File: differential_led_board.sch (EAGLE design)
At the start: 59 parts, among them IC1 SN75175SOP-16, IC10 TJA1057, IC3 LD1117S33, IC4 74LVC1G157, IC5 74LVC1G157, IC6 CD40109B, IC7 STM32F042F, IC8 AT25SF041, IC9 LT6100, J1 CORTEX_DEBUG_PTH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

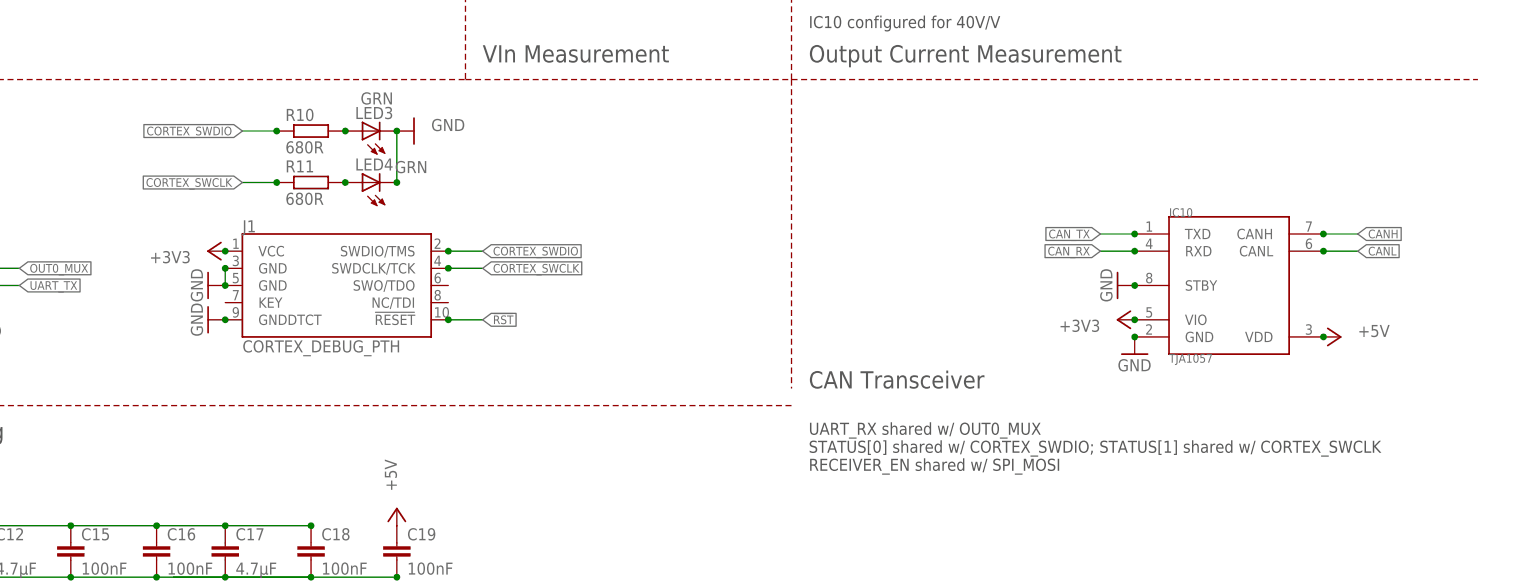
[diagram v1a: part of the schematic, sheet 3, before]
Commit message: moved status LEDs from debug pins to SPI pins
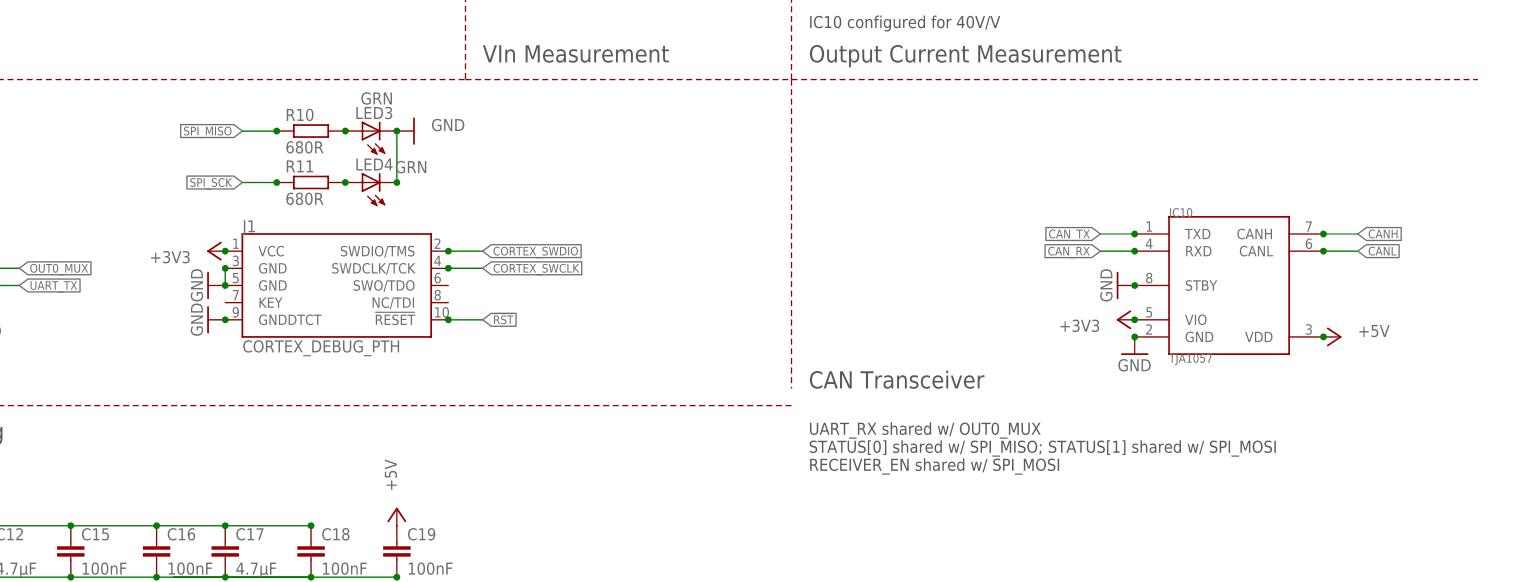
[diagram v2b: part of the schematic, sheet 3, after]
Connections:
- net CORTEX_SWCLK: no longer R11.1
- net CORTEX_SWDIO: no longer R10.1
- net SPI_MISO: now also R10.1
- net SPI_SCK: now also R11.1
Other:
- note added: "UART_RX shared w/ OUT0_MUX STATUS[0] shared w/ SPI_MISO; STATUS[1] shared w/ SPI_MOSI RECEIVER_EN shared w/ SPI_MOSI"
- note removed: "UART_RX shared w/ OUT0_MUX STATUS[0] shared w/ CORTEX_SWDIO; STATUS[1] shared w/ CORTEX_SWCLK RECEIVER_EN shared w/ SPI_MOSI"
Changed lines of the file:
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@@
 <plain>
 <text x="149.86" y="33.02" size="1.778" layer="97" align="top-left">UART_RX shared w/ OUT0_MUX
-STATUS[0] shared w/ CORTEX_SWDIO; STATUS[1] shared w/ CORTEX_SWCLK
+STATUS[0] shared w/ SPI_MISO; STATUS[1] shared w/ SPI_MOSI
 RECEIVER_EN shared w/ SPI_MOSI
 </text>
@@
 <junction x="96.52" y="58.42"/>
 </segment>
-<segment>
-<pinref part="R10" gate="G$1" pin="1"/>
-<wire x1="71.12" y1="76.2" x2="66.04" y2="76.2" width="0.1524" layer="91"/>
-<label x="66.04" y="76.2" size="1.27" layer="95" rot="R180" xref="yes"/>
-<junction x="71.12" y="76.2"/>
-</segment>
 </net>
 <net name="CORTEX_SWCLK" class="0">
@@
 <label x="101.6" y="55.88" size="1.27" layer="95" xref="yes"/>
 <junction x="96.52" y="55.88"/>
-</segment>
-<segment>
-<pinref part="R11" gate="G$1" pin="1"/>
-<label x="66.04" y="68.58" size="1.27" layer="95" rot="R180" xref="yes"/>
-<wire x1="71.12" y1="68.58" x2="66.04" y2="68.58" width="0.1524" layer="91"/>
-<junction x="71.12" y="68.58"/>
 </segment>
 </net>
@@
 <junction x="124.46" y="175.26"/>
 </segment>
+<segment>
+<pinref part="R11" gate="G$1" pin="1"/>
+<label x="66.04" y="68.58" size="1.27" layer="95" rot="R180" xref="yes"/>
+<wire x1="71.12" y1="68.58" x2="66.04" y2="68.58" width="0.1524" layer="91"/>
+<junction x="71.12" y="68.58"/>
+</segment>
 </net>
 <net name="SPI_MISO" class="0">
@@
 <junction x="124.46" y="170.18"/>
 </segment>
-</net>
+<segment>
+<pinref part="R10" gate="G$1" pin="1"/>
+<wire x1="71.12" y1="76.2" x2="66.04" y2="76.2" width="0.1524" layer="91"/>
+<label x="66.04" y="76.2" size="1.27" layer="95" rot="R180" xref="yes"/>
+<junction x="71.12" y="76.2"/>
+</segment>
+</net>

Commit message: submitted rev 1 of output and led boards to board house
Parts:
- IC1: value SN75175SOP-16 -> SN75175
- IC2: value (none) -> TLV803
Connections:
- net GND: now also IC6.D
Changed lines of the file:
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@@
 </part>
 <part name="GND20" library="supply1" library_urn="urn:adsk.eagle:library:371" deviceset="GND" device=""/>
-<part name="IC1" library="lichtenstein_onion" deviceset="SN75175" device="SOP-16"/>
+<part name="IC1" library="lichtenstein_onion" deviceset="SN75175" device="SOP-16" value="SN75175"/>
 <part name="P+3" library="supply1" library_urn="urn:adsk.eagle:library:371" deviceset="+5V" device=""/>
 <part name="GND4" library="supply1" library_urn="urn:adsk.eagle:library:371" deviceset="GND" device=""/>
@@
 <part name="+3V37" library="supply1" library_urn="urn:adsk.eagle:library:371" deviceset="+3V3" device=""/>
 <part name="GND13" library="supply1" library_urn="urn:adsk.eagle:library:371" deviceset="GND" device=""/>
-<part name="IC2" library="lichtenstein_onion" deviceset="TLV803" device="SOT-23" package3d_urn="urn:adsk.eagle:package:28738/2"/>
+<part name="IC2" library="lichtenstein_onion" deviceset="TLV803" device="SOT-23" package3d_urn="urn:adsk.eagle:package:28738/2" value="TLV803"/>
 <part name="C2" library="rcl" library_urn="urn:adsk.eagle:library:334" deviceset="C-EU" device="C0805" package3d_urn="urn:adsk.eagle:package:23617/2" value="100nF">
 <attribute name="MOUSER" value="710-885012207072"/>
@@
 </part>
 <part name="+3V33" library="supply1" library_urn="urn:adsk.eagle:library:371" deviceset="+3V3" device=""/>
+<part name="GND31" library="supply1" library_urn="urn:adsk.eagle:library:371" deviceset="GND" device=""/>
 </parts>
 <sheets>
@@
 <attribute name="VALUE" x="114.3" y="142.24" size="1.778" layer="96" rot="R270"/>
 </instance>
+<instance part="GND31" gate="1" x="116.84" y="152.4" smashed="yes" rot="R270">
+<attribute name="VALUE" x="114.3" y="154.94" size="1.778" layer="96" rot="R270"/>
+</instance>
 </instances>
 <busses>
@@
 <junction x="119.38" y="139.7"/>
 </segment>
-</net>
+<segment>
+<pinref part="IC6" gate="G$1" pin="D"/>
+<pinref part="GND31" gate="1" pin="GND"/>
+<junction x="119.38" y="152.4"/>
+</segment>
+</net>
